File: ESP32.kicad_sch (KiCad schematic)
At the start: 10 parts, among them J201 GPIO, J203 Conn_01x01, J302 Conn_01x02, U201 ESP32-WROOM-32E-N16

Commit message: Redo schematics
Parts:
- removed D1101, D1102: BAT54A, Package_TO_SOT_SMD:SOT-323_SC-70, symbol Diode:BAT54A
- removed J201: GPIO, Connector_PinHeader_2.54mm:PinHeader_2x10_P2.54mm_Vertical, symbol Connector_Generic:Conn_02x10_Odd_Even
- removed J203: Conn_01x01, TestPoint:TestPoint_Pad_D2.0mm, symbol Connector_Generic:Conn_01x01
- removed J302: Conn_01x02, Connector_PinHeader_2.54mm:PinHeader_1x02_P2.54mm_Vertical, symbol Connector_Generic:Conn_01x02
- removed U201: ESP32-WROOM-32E-N16, RF_Module:ESP32-WROOM-32, symbol RF_Module:ESP32-WROOM-32
- added C301, C302: 100nF/50V, PCM_Capacitor_SMD_AKL:C_0603_1608Metric, symbol Device:C_Small
- added C305: 100nF, PCM_Capacitor_SMD_AKL:C_0402_1005Metric, symbol Device:C
- added D301: RED LED, PCM_LED_SMD_AKL:LED_0603_1608Metric, symbol Device:LED
- added D302, D303: GREEN LED, PCM_LED_SMD_AKL:LED_0603_1608Metric, symbol Device:LED
- added J301: GPIO, Connector_PinHeader_2.54mm:PinHeader_2x10_P2.54mm_Vertical, symbol Connector_Generic:Conn_02x10_Odd_Even
- added LED301: SK68XX-MINI-HS, PCM_LED_SMD_AKL:LED_SK6812MINI_PLCC4_3.5x3.5mm_P1.75mm, symbol HALSER:SK68XX-MINI-HS
- added R303: 2k, PCM_Resistor_SMD_AKL:R_0402_1005Metric, symbol Device:R
- added R304, R305: 1.5k, PCM_Resistor_SMD_AKL:R_0402_1005Metric, symbol Device:R
- added R306: 0R, PCM_Resistor_SMD_AKL:R_0603_1608Metric, symbol Device:R
- added SW301, SW302: SW_Push, Button_Switch_SMD:SW_SPST_TL3342, symbol Switch:SW_Push
- added U301: ESP32-C3-MINI-1, PCM_Espressif:ESP32-C3-MINI-1, symbol PCM_Espressif:ESP32-C3-MINI-1
- C303: renamed from C203; footprint Capacitor_SMD:C_0402_1005Metric -> PCM_Capacitor_SMD_AKL:C_0402_1005Metric
- C304: renamed from C202; value 22uF -> 10uF/25V; footprint Capacitor_SMD:C_0603_1608Metric -> PCM_Capacitor_SMD_AKL:C_0805_2012Metric; LCSC C59461 -> C15850; Notes Min 6.3V -> (none)
- R301: renamed from R1103; footprint Resistor_SMD:R_0402_1005Metric -> PCM_Resistor_SMD_AKL:R_0402_1005Metric
- R302: renamed from R201; footprint Resistor_SMD:R_0402_1005Metric -> PCM_Resistor_SMD_AKL:R_0402_1005Metric
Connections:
- net +3.3V: now also C305.1, J301.18 (Pin_18), J301.3 (Pin_3), LED301.3 (VCC), R303.1, R304.1, R305.1, U301.3 (3V3)
- net CAN_RX: now also D302.1 (K), J301.4 (Pin_4), U301.19 (GPIO5/ADC2_CH0)
- net CAN_TX: now also D303.1 (K), J301.2 (Pin_2), U301.18 (GPIO4/ADC1_CH4)
- net DQ: now also J301.15 (Pin_15), U301.16 (GPIO10)
- net GND: now also C301.2, C302.2, C305.2, D301.1 (K), J301.1 (Pin_1), J301.12 (Pin_12), J301.13 (Pin_13), J301.20 (Pin_20), J301.6 (Pin_6), LED301.1 (GND), SW301.1, SW302.1, U301.1 (GND), U301.11 (GND), U301.14 (GND), U301.2 (GND), U301.36 (GND), U301.37 (GND), U301.38 (GND), U301.39 (GND), U301.40 (GND), U301.41 (GND), U301.42 (GND), U301.43 (GND), U301.44 (GND), U301.45 (GND), U301.46 (GND), U301.47 (GND), U301.48 (GND), U301.49 (GND), U301.50 (GND), U301.51 (GND), U301.52 (GND), U301.53 (GND)
- net SCL: now also J301.19 (Pin_19), U301.21 (GPIO7)
- net SDA: now also J301.17 (Pin_17), U301.20 (GPIO6)
- net EN renamed CHIP_PU
- net CHIP_PU: now also C302.1, SW302.2, U301.8 (EN/CHIP_PU)
- net IO0 renamed GPIO8
- net GPIO8: now also J301.8 (Pin_8), R306.1, U301.22 (GPIO8)
- new net: D301.2 (A), R303.2
- new net: D303.2 (A), R305.2
- new net: D302.2 (A), R304.2
- new net GPIO0: J301.5 (Pin_5), U301.12 (GPIO0/ADC1_CH0/XTAL_32K_P)
- new net GPIO1: J301.7 (Pin_7), U301.13 (GPIO1/ADC1_CH1/XTAL_32K_N)
- new net GPIO20: J301.14 (Pin_14), U301.30 (GPIO20/U0RXD)
- new net GPIO21: J301.16 (Pin_16), U301.31 (GPIO21/U0TXD)
- new net GPIO9: C301.1, J301.10 (Pin_10), SW301.2, U301.23 (GPIO9)
- new net RGB_CTRL: LED301.2 (DIN), R306.2
- new net SER_RX: J301.9 (Pin_9), U301.5 (GPIO2/ADC1_CH2)
- new net SER_TX: J301.11 (Pin_11), U301.6 (GPIO3/ADC1_CH3)
- new net USB_D+: U301.27 (GPIO19/USB_D+)
- new net USB_D-: U301.26 (GPIO18/USB_D-)
- no-connect marks 6 -> 1
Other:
- note added: "Boot"
- note added: "LEDs"
- note added: "Push buttons"
- note added: "RGB LED control"
- note added: "Reset"
- note added: "Strapping"
- note removed: "CAP here to slowdown reset on poweron"
- note removed: "For safety reasons, a USB 5V two-pin header was downgraded to a single pin test point."
- note removed: "From Espressif Ethernet Reference board"
- note removed: "JTAG"
- note removed: "Strap"
- moved on the sheet: C303, C304, R301, R302

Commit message: Further design adjustments
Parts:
- R306: footprint PCM_Resistor_SMD_AKL:R_0603_1608Metric -> PCM_Resistor_SMD_AKL:R_0603_1608Metric_Pad0.98x0.95mm_HandSolder
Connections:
- net +3.3V: now also D302.2 (A); no longer R304.1
- net CAN_RX: now also R304.2; no longer D302.1 (K)
- net DQ: no longer J301.15 (Pin_15)
- net GPIO0: now also J301.17 (Pin_17); no longer J301.5 (Pin_5)
- net GPIO1: now also J301.19 (Pin_19); no longer J301.7 (Pin_7)
- net SCL: no longer J301.19 (Pin_19)
- net SDA: no longer J301.17 (Pin_17)
- new net: D302.1 (K), R304.1
- new net DQ_C: J301.15 (Pin_15)
- new net SCL_C: J301.5 (Pin_5)
- new net SDA_C: J301.7 (Pin_7)
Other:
- moved on the sheet: D302, R304
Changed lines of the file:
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@@
 	)
 	(label "GPIO1"
-		(at 231.14 38.1 180)
+		(at 231.14 53.34 180)
 		(fields_autoplaced yes)
 		(effects
@@
 	)
 	(label "GPIO0"
-		(at 231.14 35.56 180)
+		(at 231.14 50.8 180)
 		(fields_autoplaced yes)
 		(effects
@@
 		)
 	)
-	(hierarchical_label "SDA"
+	(hierarchical_label "SDA_C"
 		(shape bidirectional)
-		(at 231.14 50.8 180)
+		(at 231.14 38.1 180)
 		(fields_autoplaced yes)
 		(effects
@@
 		)
 	)
-	(hierarchical_label "SCL"
+	(hierarchical_label "SCL_C"
 		(shape output)
-		(at 231.14 53.34 180)
+		(at 231.14 35.56 180)
 		(fields_autoplaced yes)
 		(effects
@@
 		)
 	)
-	(hierarchical_label "DQ"
+	(hierarchical_label "DQ_C"
 		(shape bidirectional)
 		(at 231.14 48.26 180)
@@
 			)
 		)
-		(property "Footprint" "PCM_Resistor_SMD_AKL:R_0603_1608Metric"
+		(property "Footprint" "PCM_Resistor_SMD_AKL:R_0603_1608Metric_Pad0.98x0.95mm_HandSolder"
 			(at 172.72 154.178 90)
 			(effects
@@
 	(symbol
 		(lib_id "Device:LED")
-		(at 133.35 165.1 90)
+		(at 133.35 154.94 90)
 		(unit 1)
 		(exclude_from_sim no)
@@
 		(dnp no)
 		(property "Reference" "D302"
-			(at 136.3472 164.1094 90)
+			(at 136.3472 153.9494 90)
 			(effects
 				(font
@@
 		)
 		(property "Value" "GREEN LED"
-			(at 136.3472 166.4208 90)
+			(at 136.3472 156.2608 90)
 			(effects
 				(font
@@
 		)
 		(property "Footprint" "PCM_LED_SMD_AKL:LED_0603_1608Metric"
-			(at 133.35 165.1 0)
+			(at 133.35 154.94 0)
 			(effects
 				(font
@@
 		)
 		(property "Datasheet" "~"
-			(at 133.35 165.1 0)
+			(at 133.35 154.94 0)
 			(effects
 				(font
@@
 		)
 		(property "Description" ""
-			(at 133.35 165.1 0)
+			(at 133.35 154.94 0)
 			(effects
 				(font
@@
 		)
 		(property "LCSC" "C965804"
-			(at 133.35 165.1 0)
+			(at 133.35 154.94 0)
 			(effects
 				(font
@@
 		)
 		(property "Sim.Device" ""
-			(at 133.35 165.1 0)
+			(at 133.35 154.94 0)
 			(effects
 				(font
@@
 		)
 		(property "Sim.Pins" ""
-			(at 133.35 165.1 0)
+			(at 133.35 154.94 0)
 			(effects
 				(font
@@
 		)
 		(property "Note" ""
-			(at 133.35 165.1 0)
+			(at 133.35 154.94 0)
 			(effects
 				(font
@@
 	(symbol
 		(lib_id "Device:R")
-		(at 133.35 154.94 0)
+		(at 133.35 165.1 0)
 		(unit 1)
 		(exclude_from_sim no)
@@
 		(dnp no)
 		(property "Reference" "R304"
-			(at 135.128 153.7716 0)
+			(at 135.128 163.9316 0)
 			(effects
 				(font
@@
 		)
 		(property "Value" "1.5k"
-			(at 135.128 156.083 0)
+			(at 135.128 166.243 0)
 			(effects
 				(font
@@
 		)
 		(property "Footprint" "PCM_Resistor_SMD_AKL:R_0402_1005Metric"
-			(at 131.572 154.94 90)
+			(at 131.572 165.1 90)
 			(effects
 				(font
@@
 		)
 		(property "Datasheet" "~"
-			(at 133.35 154.94 0)
+			(at 133.35 165.1 0)
 			(effects
 				(font
@@
 		)
 		(property "Description" ""
-			(at 133.35 154.94 0)
+			(at 133.35 165.1 0)
 			(effects
 				(font
@@
 		)
 		(property "LCSC" "C25867"
-			(at 133.35 154.94 0)
+			(at 133.35 165.1 0)
 			(effects
 				(font
@@
 		)
 		(property "Sim.Device" ""
-			(at 133.35 154.94 0)
+			(at 133.35 165.1 0)
 			(effects
 				(font
@@
 		)
 		(property "Sim.Pins" ""
-			(at 133.35 154.94 0)
+			(at 133.35 165.1 0)
 			(effects
 				(font
@@
 		)
 		(property "Note" ""
-			(at 133.35 154.94 0)
+			(at 133.35 165.1 0)
 			(effects
 				(font

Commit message: Further manufacturing tweaks
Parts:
- J301: JLCPCB_CORRECTION (none) -> 1.27;11.43;90; LCSC C492427 -> C7501600
- LED301: JLCPCB_CORRECTION (none) -> 0;0;180
- U301: JLCPCB_CORRECTION (none) -> 0;2.7;0
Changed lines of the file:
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@@
+			)
+		)
+		(property "JLCPCB_CORRECTION" "0;2.7;0"
+			(at 144.78 74.93 0)
+			(effects
+				(font
+					(size 1.27 1.27)
+				)
+				(hide yes)
 			)
 		)
@@
 			)
 		)
-		(property "LCSC" "C492427"
+		(property "LCSC" "C7501600"
 			(at 236.22 40.64 0)
 			(effects
@@
 		)
 		(property "Note" ""
+			(at 236.22 40.64 0)
+			(effects
+				(font
+					(size 1.27 1.27)
+				)
+				(hide yes)
+			)
+		)
+		(property "JLCPCB_CORRECTION" "1.27;11.43;90"
 			(at 236.22 40.64 0)
 			(effects
@@
 			(at 193.04 153.67 0)
 			(effects
+				(font
+					(size 1.27 1.27)
+				)
+				(hide yes)
+			)
+		)
+		(property "JLCPCB_CORRECTION" "0;0;180"
+			(at 193.04 153.67 0)
+			(effects

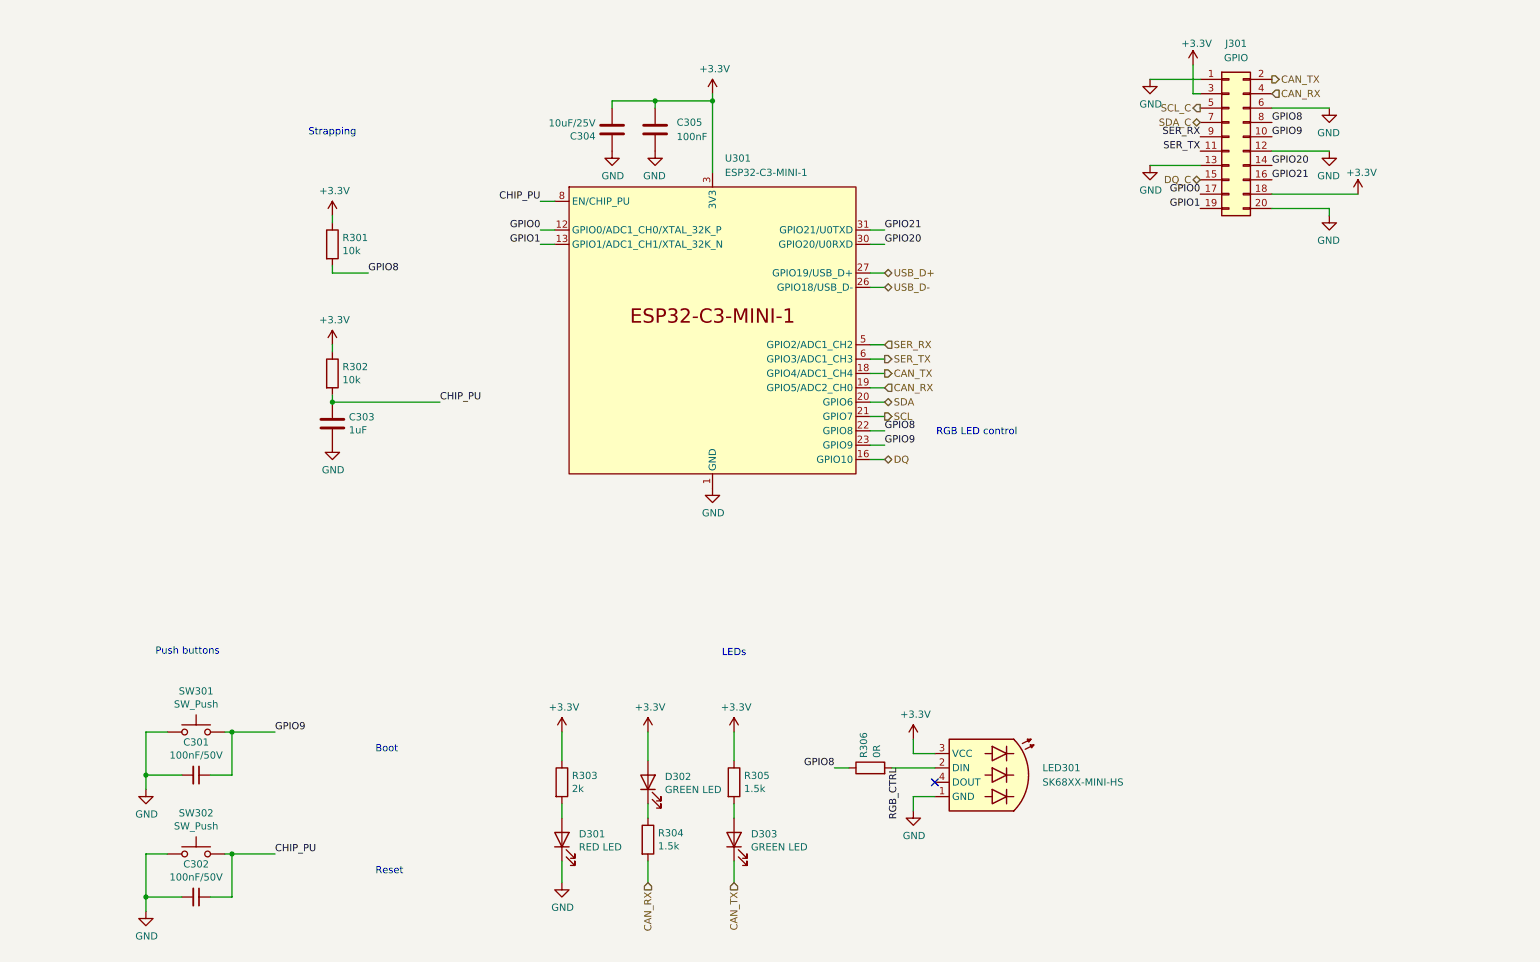
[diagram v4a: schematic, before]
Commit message: Add a hall effect sensor
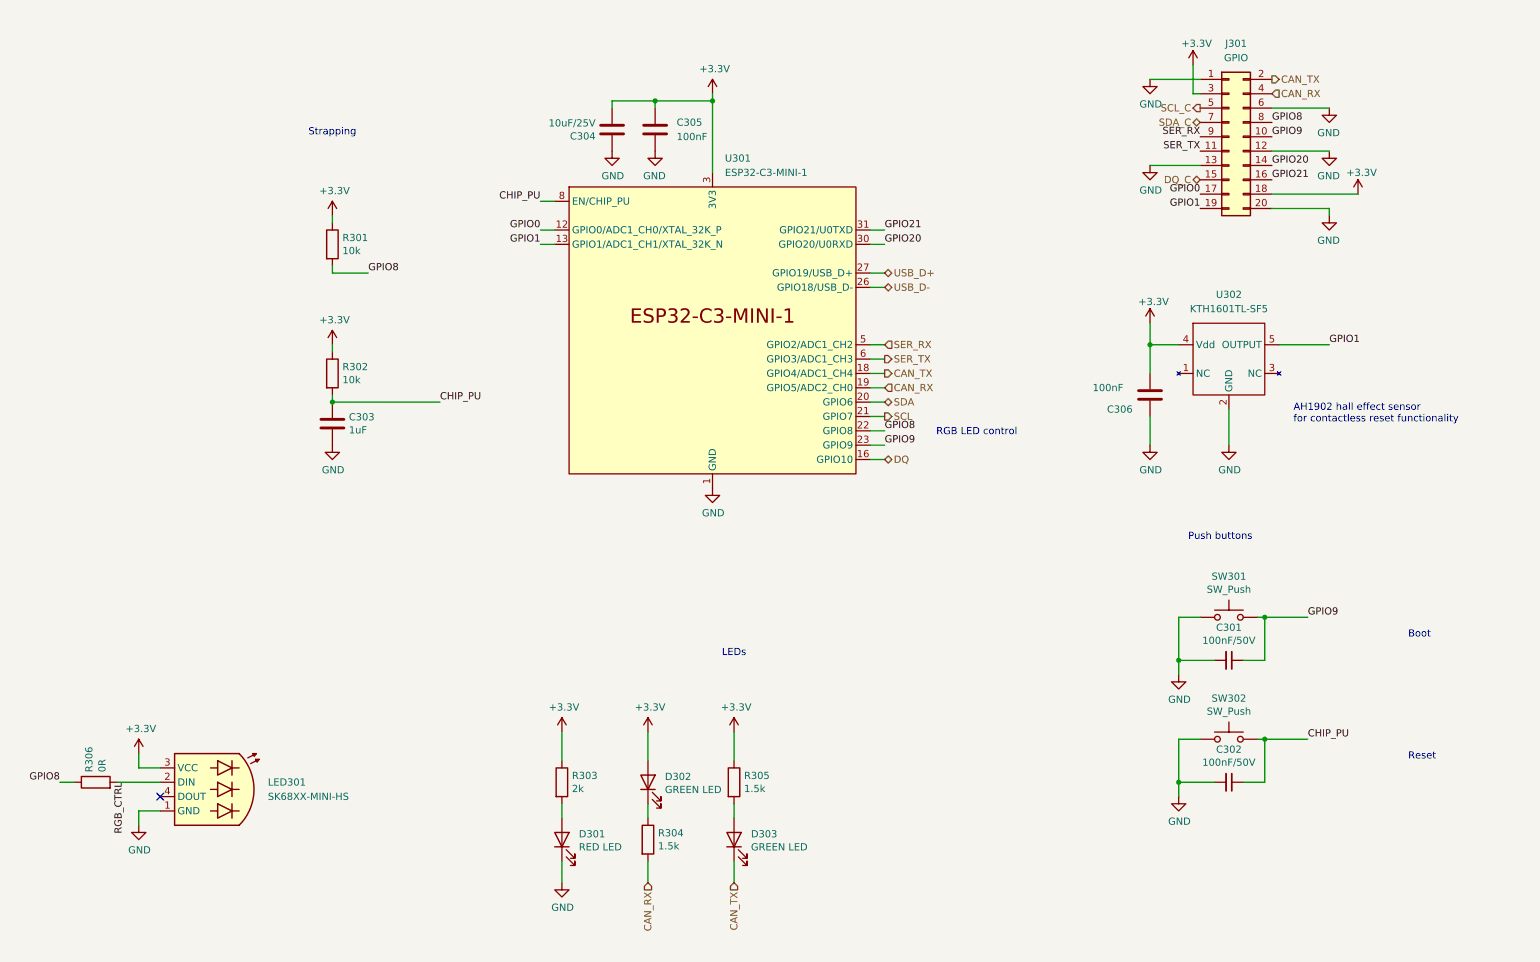
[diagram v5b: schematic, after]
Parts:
- added C306: 100nF, Capacitor_SMD:C_0402_1005Metric, symbol Device:C
- added U302: KTH1601TL-SF5, PCM_Package_TO_SOT_SMD_AKL:SOT-553, symbol SH-wg:AH1902
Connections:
- net +3.3V: now also C306.2, U302.4 (Vdd)
- net GND: now also C306.1, U302.2 (GND)
- net GPIO1: now also U302.5 (OUTPUT)
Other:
- note added: "AH1902 hall effect sensor for contactless reset functionality"
- company: Hat Labs Ltd -> Hat Labs oy
- title: Hat Labs Marine Engine & Tank interface (HALMET) -> Hat Labs Serial Interface Device (HALSER)
- moved on the sheet: C301, C302, LED301, R306, SW301, SW302

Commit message: Fix issues found in -a1
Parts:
- added R307: 10k, Resistor_SMD:R_0402_1005Metric, symbol Device:R
- C301, C302: footprint PCM_Capacitor_SMD_AKL:C_0603_1608Metric -> Capacitor_SMD:C_0603_1608Metric
- C303, C305: footprint PCM_Capacitor_SMD_AKL:C_0402_1005Metric -> Capacitor_SMD:C_0402_1005Metric
- C304: footprint PCM_Capacitor_SMD_AKL:C_0805_2012Metric -> Capacitor_SMD:C_0805_2012Metric
- D301, D302, D303: footprint PCM_LED_SMD_AKL:LED_0603_1608Metric -> LED_SMD:LED_0603_1608Metric
- LED301: value SK68XX-MINI-HS -> SK6805-MICRO-J; footprint PCM_LED_SMD_AKL:LED_SK6812MINI_PLCC4_3.5x3.5mm_P1.75mm -> HALSER:LED_SK6805_PLCC4_2.4x2.7mm_P1.3mm; LCSC C2922787 -> C2909056
- R301, R302, R303, R304, R305: footprint PCM_Resistor_SMD_AKL:R_0402_1005Metric -> Resistor_SMD:R_0402_1005Metric
- R306: value 0R -> 470R; footprint PCM_Resistor_SMD_AKL:R_0603_1608Metric_Pad0.98x0.95mm_HandSolder -> Resistor_SMD:R_0603_1608Metric; LCSC C21189 -> (none)
- U302: footprint PCM_Package_TO_SOT_SMD_AKL:SOT-553 -> Package_TO_SOT_SMD:SOT-553
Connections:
- net +3.3V: now also R307.1
- net GPIO9: now also R307.2
- net SER_RX: now also U301.6 (GPIO3/ADC1_CH3); no longer U301.5 (GPIO2/ADC1_CH2)
- net SER_TX: now also U301.5 (GPIO2/ADC1_CH2); no longer U301.6 (GPIO3/ADC1_CH3)
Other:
- note added: "Button input"

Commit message: Bump versions
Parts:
- U302: symbol SH-wg:AH1902 -> HALSER:AH1902
- renumbered C303 to C301, C304 to C302, C305 to C303, C306 to C304, C301 to C305, C302 to C306, R306 to R301, R307 to R302, R301 to R303, R302 to R304, R303 to R305, R304 to R306, R305 to R307
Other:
- note added: "Hall effect sensor for contactless restart and reset functionality"
- note removed: "AH1902 hall effect sensor for contactless reset functionality"
